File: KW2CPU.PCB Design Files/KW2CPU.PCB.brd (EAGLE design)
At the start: 50 x 30 mm, 67 parts, among them IC1 25AA080SN, J1 DF12_M, J2 MOLEX55560-0207, J3 MMCX_VERT, U1 MKW21D, U3 RF6555, U5 F-ANTENNA, X1 32KHZ, X2 32MHZ

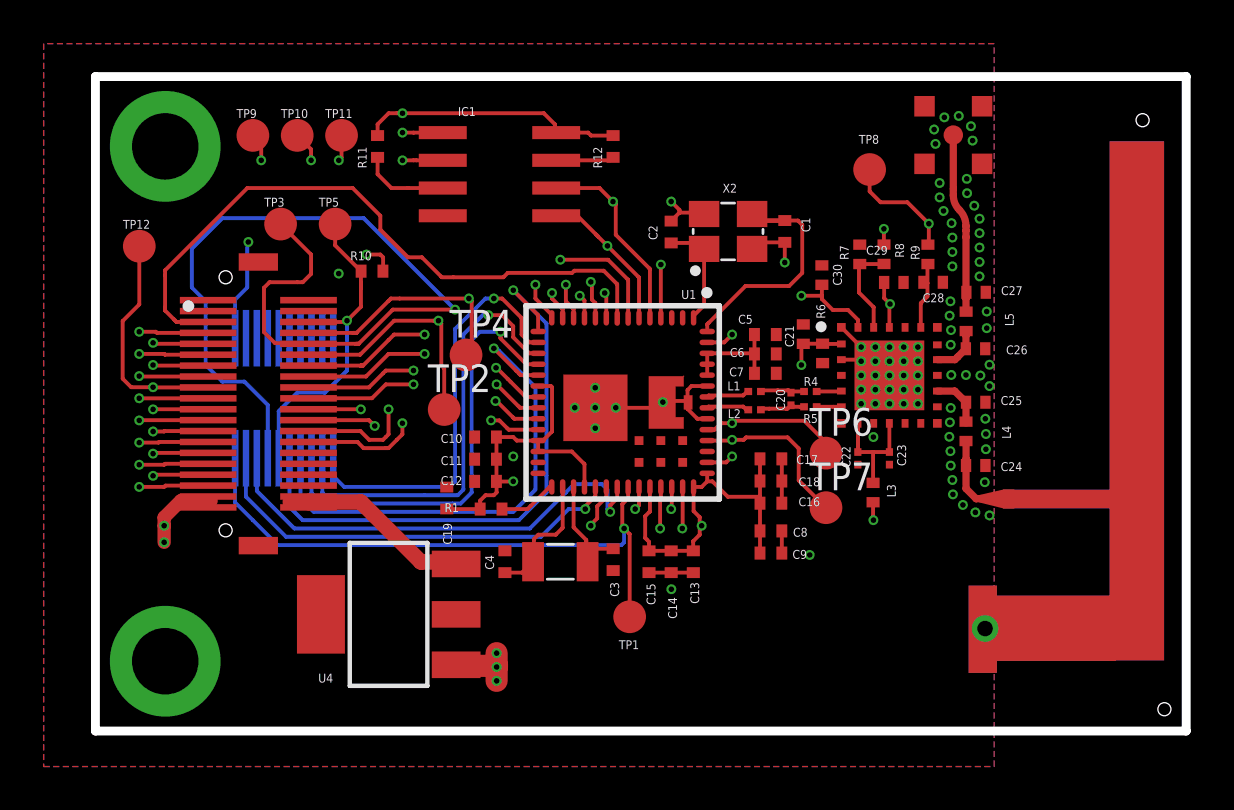
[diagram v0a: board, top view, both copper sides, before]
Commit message: Added part numbers and manufacturers (inconsistent)
Also moved files to proper directories. Needs manual inconsistency
fixing
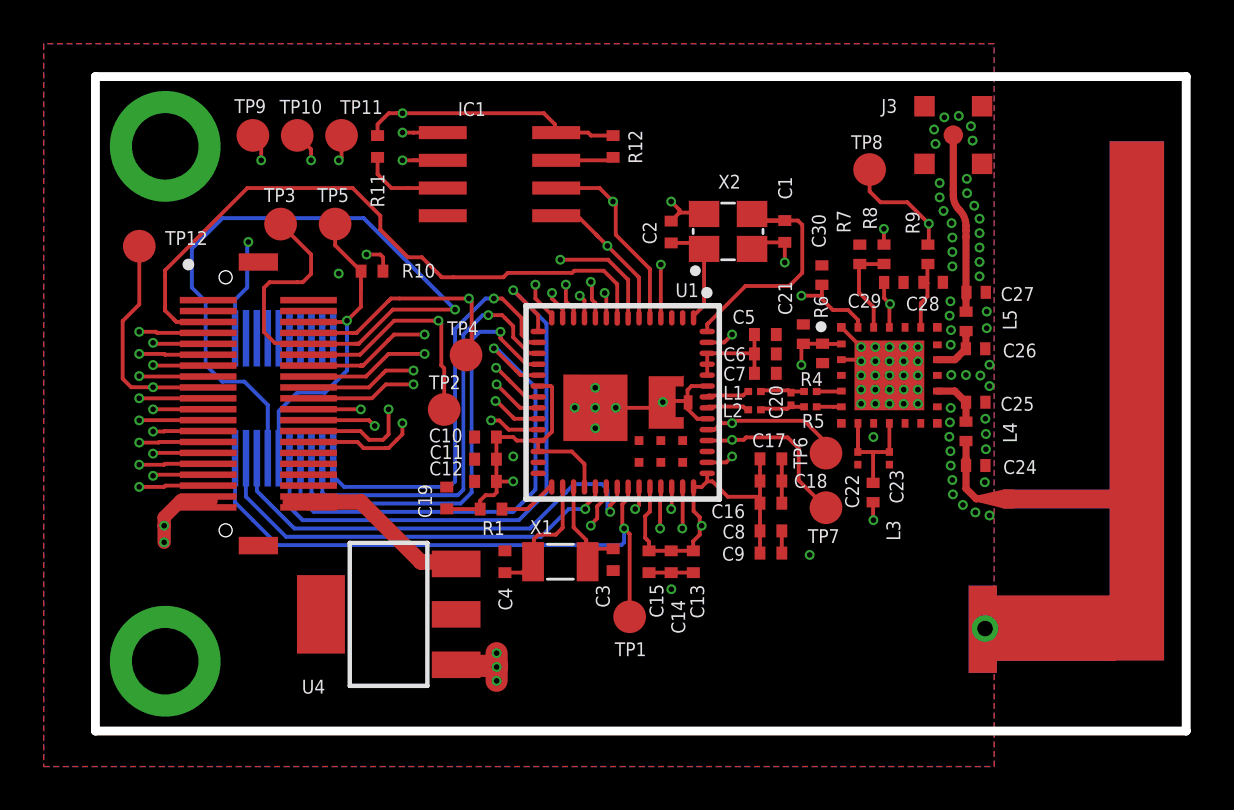
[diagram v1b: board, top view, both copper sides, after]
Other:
- board text added: "R.S 11/22/14"

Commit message: Exporting production files in progress
Creating production files. Missing: ECO, Stackup, Drill
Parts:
- C20: value (none) -> 1.2pF
- C21, C28, C29, C30: value (none) -> 8pF
- C22: value (none) -> 1uF
- C23: value (none) -> 5.1pF
- C25: value (none) -> 0.2pF
- L1, L2: value (none) -> 1nH
- L3: value (none) -> 100Ohm Ferrite
- L4: value (none) -> 2.2nH
- L5, R4, R5, R7, R8, R9: value (none) -> 0
- R6: value (none) -> 51k
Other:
- board text added: "KW2CPU.PCB.v1.0"
- board text removed: "KW2CPU.v1.0"
